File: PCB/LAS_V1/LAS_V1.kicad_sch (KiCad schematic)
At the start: 14 parts, among them J1 Screw_Terminal_01x02, J2 Screw_Terminal_01x03, K2 SANYOU_SRD_Form_C, Q1 NPN, U1 XL1509-5.0

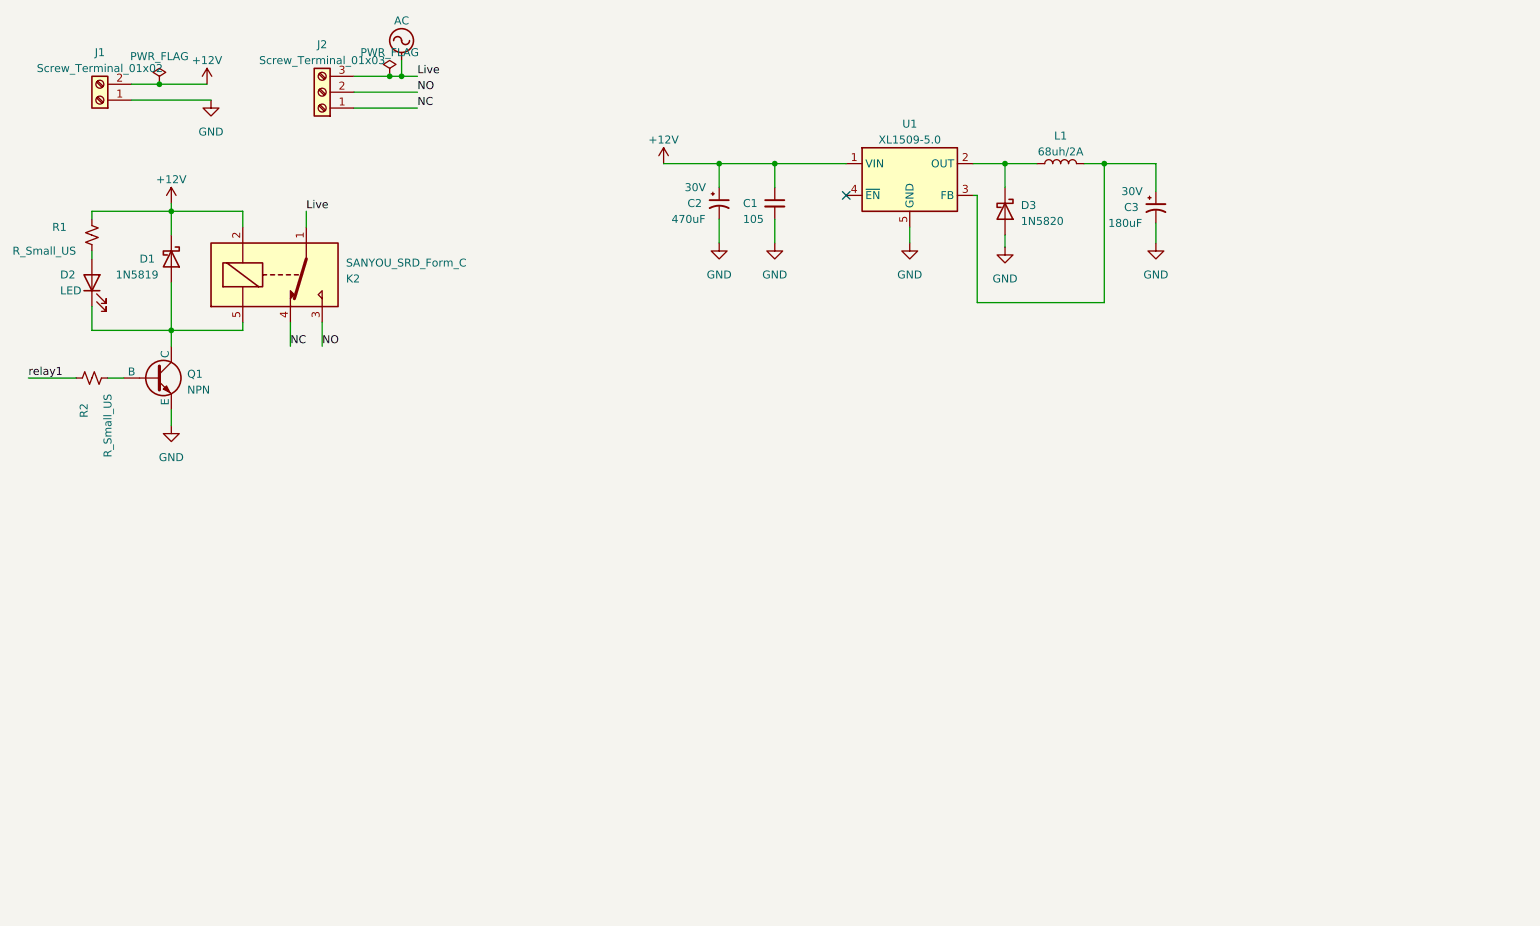
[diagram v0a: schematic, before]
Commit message: Added more relay components, LEDS, Clearing Up
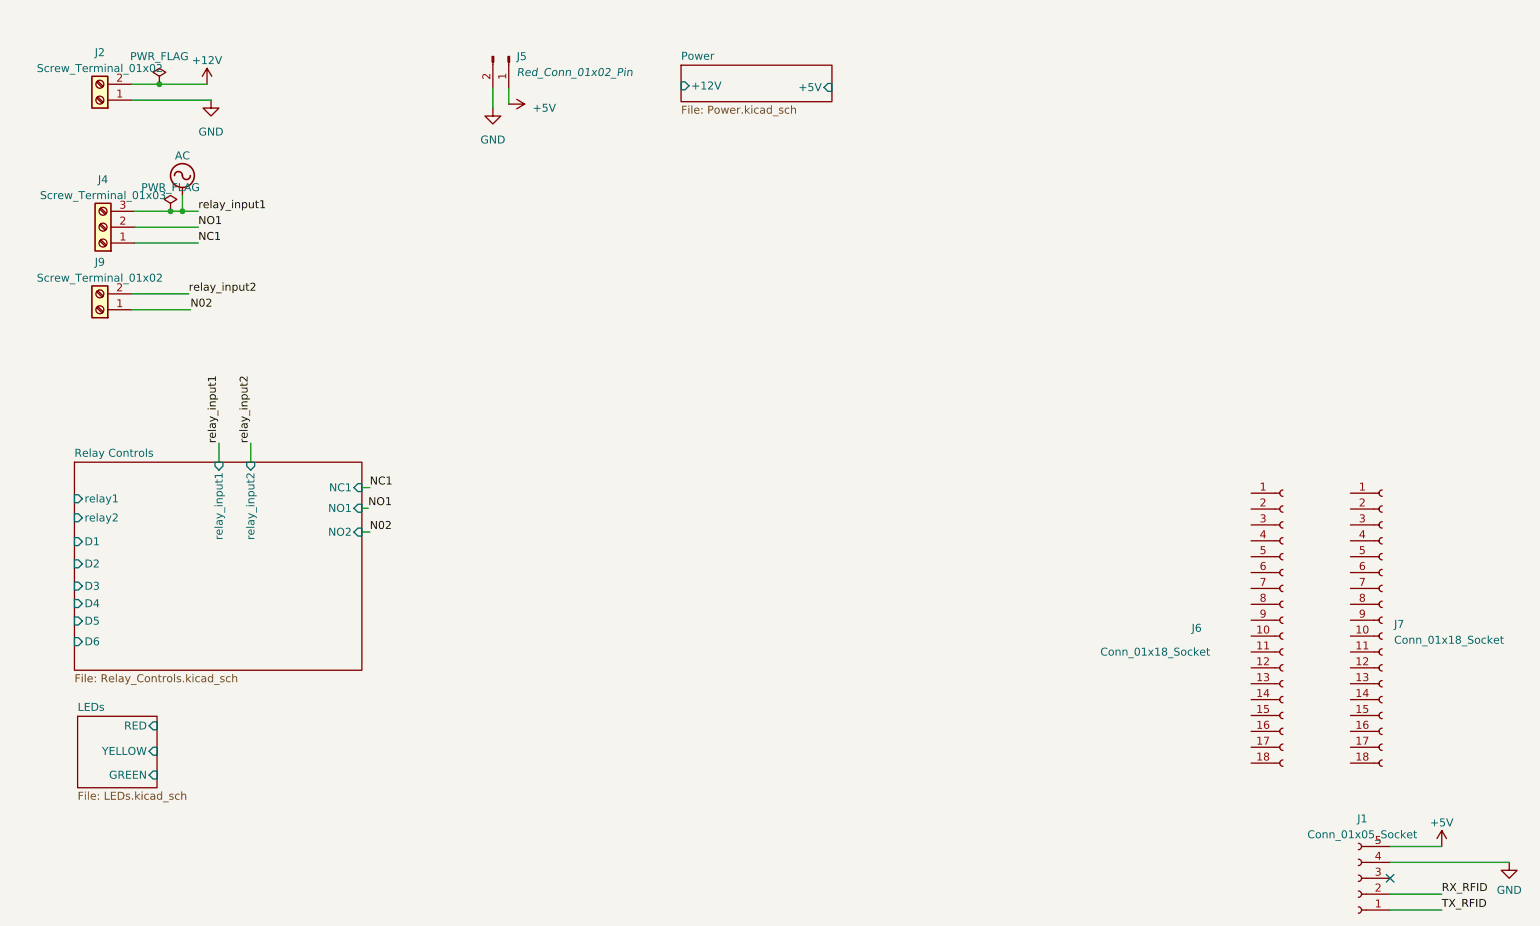
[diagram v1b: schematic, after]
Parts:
- removed C1: 105, symbol Device:C_Small
- removed C2: 470uF, symbol Device:C_Polarized_Small_US
- removed C3: 180uF, symbol Device:C_Polarized_Small_US
- removed D1: 1N5819, Diode_THT:D_DO-41_SOD81_P10.16mm_Horizontal, symbol Diode:1N5819
- removed D2: LED, symbol Device:LED
- removed D3: 1N5820, Diode_THT:D_DO-201AD_P15.24mm_Horizontal, symbol Diode:1N5820
- removed J2: Screw_Terminal_01x03, symbol Connector:Screw_Terminal_01x03
- removed K2: SANYOU_SRD_Form_C, Relay_THT:Relay_SPDT_SANYOU_SRD_Series_Form_C, symbol Relay:SANYOU_SRD_Form_C
- removed L1: 68uh/2A, symbol Device:L
- removed Q1: NPN, symbol Simulation_SPICE:NPN
- removed R1, R2: R_Small_US, symbol Device:R_Small_US
- removed U1: XL1509-5.0, Package_SO:SOIC-8_3.9x4.9mm_P1.27mm, symbol Regulator_Switching:XL1509-5.0
- added J1: Conn_01x05_Socket, symbol Connector:Conn_01x05_Socket
- added J4: Screw_Terminal_01x03, symbol Connector:Screw_Terminal_01x03
- added J5: Red_Conn_01x02_Pin, symbol Connector:Conn_01x02_Pin
- added J6, J7: Conn_01x18_Socket, symbol Connector:Conn_01x18_Socket
- added J9: Screw_Terminal_01x02, symbol Connector:Screw_Terminal_01x02
- renumbered J1 to J2
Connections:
- net AC: now also J4.3 (Pin_3)
- net GND: now also J1.4 (Pin_4), J5.2 (Pin_2)
- new net +5V: J1.5 (Pin_5), J5.1 (Pin_1)
- new net N02: J9.1 (Pin_1)
- new net NC1: J4.1 (Pin_1)
- new net NO1: J4.2 (Pin_2)
- new net RX_RFID: J1.2 (Pin_2)
- new net TX_RFID: J1.1 (Pin_1)
- new net relay_input2: J9.2 (Pin_2)
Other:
- added sheet LEDs (LEDs.kicad_sch)
- added sheet Power (Power.kicad_sch)
- added sheet Relay Controls (Relay_Controls.kicad_sch)
